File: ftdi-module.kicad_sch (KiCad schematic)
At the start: 49 parts, among them J1 USB3106-30-0230-A, U2 ISO1641, U3 NCP163ASN330T1G, U5 FT4232H-56Q, Y1 KX-7_12,MHz

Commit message: Loclib
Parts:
- U5: footprint antmicro-footprints:QFN-56-1EP_8x8mm_P0.5mm_EP5.5.9x5.9mm -> nuc-compute-cluster-power-breakout-footprints:QFN-56-1EP_8x8mm_P0.5mm_EP5.5.9x5.9mm; symbol antmicroInterfaceControllers:FT4232H-56Q -> nuc-compute-cluster-power-breakout:FT4232H-56Q
- WP1: footprint antmicro-footprints:Testpoint_smd_1mm -> nuc-compute-cluster-power-breakout-footprints:Testpoint_smd_1mm; symbol antmicroTestPoints:TP_SMD1MM -> nuc-compute-cluster-power-breakout:TP_SMD1MM

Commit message: Update README
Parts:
- 3V3, 3V3_USB1, 5V_USB1, SCL1, SCL_FTDI1, SDA1, SDA_FTDI1, WP1: footprint nuc-compute-cluster-power-breakout-footprints:Testpoint_smd_1mm -> d1600e-psu-breakout-board-footprints:Testpoint_smd_1mm; symbol nuc-compute-cluster-power-breakout:TP_SMD1MM -> d1600e-psu-breakout-board:TP_SMD1MM
- C1, C2: footprint nuc-compute-cluster-power-breakout-footprints:0402-cap -> d1600e-psu-breakout-board-footprints:0402-cap; symbol nuc-compute-cluster-power-breakout:C_27p_0402 -> d1600e-psu-breakout-board:C_27p_0402
- C10, C14, C15, C16, C17, C18, C3, C4, C6, C7, C8, C9: footprint nuc-compute-cluster-power-breakout-footprints:0402-cap -> d1600e-psu-breakout-board-footprints:0402-cap; symbol nuc-compute-cluster-power-breakout:C_100n_0402 -> d1600e-psu-breakout-board:C_100n_0402
- C11, C12, C13, C19, C20: footprint nuc-compute-cluster-power-breakout-footprints:0402-cap -> d1600e-psu-breakout-board-footprints:0402-cap; symbol nuc-compute-cluster-power-breakout:C_4u7_0402 -> d1600e-psu-breakout-board:C_4u7_0402
- D1: footprint nuc-compute-cluster-power-breakout-footprints:TPD2E009DRTR -> d1600e-psu-breakout-board-footprints:TPD2E009DRTR; symbol nuc-compute-cluster-power-breakout:PESD5V0S2BQA -> d1600e-psu-breakout-board:PESD5V0S2BQA
- D2: footprint nuc-compute-cluster-power-breakout-footprints:LED_0603 -> d1600e-psu-breakout-board-footprints:LED_0603; symbol nuc-compute-cluster-power-breakout:LG_L29K-G2J1-24-Z -> d1600e-psu-breakout-board:LG_L29K-G2J1-24-Z
- FB1, FB2, FB3: footprint nuc-compute-cluster-power-breakout-footprints:0603 -> d1600e-psu-breakout-board-footprints:0603; symbol nuc-compute-cluster-power-breakout:BLM18AG601SN1D -> d1600e-psu-breakout-board:BLM18AG601SN1D
- J1: footprint nuc-compute-cluster-power-breakout-footprints:usb3106-30-0230 -> d1600e-psu-breakout-board-footprints:usb3106-30-0230; symbol nuc-compute-cluster-power-breakout:USB3106-30-0230-A -> d1600e-psu-breakout-board:USB3106-30-0230-A
- R1: footprint nuc-compute-cluster-power-breakout-footprints:0402-res -> d1600e-psu-breakout-board-footprints:0402-res; symbol nuc-compute-cluster-power-breakout:R_1k_0402 -> d1600e-psu-breakout-board:R_1k_0402
- R3: footprint nuc-compute-cluster-power-breakout-footprints:0402-res -> d1600e-psu-breakout-board-footprints:0402-res; symbol nuc-compute-cluster-power-breakout:R_12k_0402 -> d1600e-psu-breakout-board:R_12k_0402
- R36, R37, R5, R6: footprint nuc-compute-cluster-power-breakout-footprints:0402-res -> d1600e-psu-breakout-board-footprints:0402-res; symbol nuc-compute-cluster-power-breakout:R_1k5_0402 -> d1600e-psu-breakout-board:R_1k5_0402
- R38, R39, R4, R42, R8: footprint nuc-compute-cluster-power-breakout-footprints:0603-res -> d1600e-psu-breakout-board-footprints:0603-res; symbol nuc-compute-cluster-power-breakout:R_0R_0603 -> d1600e-psu-breakout-board:R_0R_0603
- R7: footprint nuc-compute-cluster-power-breakout-footprints:0402-res -> d1600e-psu-breakout-board-footprints:0402-res; symbol nuc-compute-cluster-power-breakout:R_330R_0402 -> d1600e-psu-breakout-board:R_330R_0402
- U2: footprint nuc-compute-cluster-power-breakout-footprints:SOIC-8_W3.9mm -> d1600e-psu-breakout-board-footprints:SOIC-8_W3.9mm; symbol nuc-compute-cluster-power-breakout:ISO1641 -> d1600e-psu-breakout-board:ISO1641
- U3: footprint nuc-compute-cluster-power-breakout-footprints:SOT-23-5 -> d1600e-psu-breakout-board-footprints:SOT-23-5; symbol nuc-compute-cluster-power-breakout:NCP163ASN330T1G -> d1600e-psu-breakout-board:NCP163ASN330T1G
- U5: footprint nuc-compute-cluster-power-breakout-footprints:QFN-56-1EP_8x8mm_P0.5mm_EP5.5.9x5.9mm -> d1600e-psu-breakout-board-footprints:QFN-56-1EP_8x8mm_P0.5mm_EP5.5.9x5.9mm; symbol nuc-compute-cluster-power-breakout:FT4232H-56Q -> d1600e-psu-breakout-board:FT4232H-56Q
- Y1: footprint nuc-compute-cluster-power-breakout-footprints:KX-7 -> d1600e-psu-breakout-board-footprints:KX-7; symbol nuc-compute-cluster-power-breakout:KX-7_12,MHz -> d1600e-psu-breakout-board:KX-7_12,MHz
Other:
- note added: "Filtering"
- note added: "I2C separation"
- note removed: "Filtration"
- note removed: "Transmission Lines Separation"
- company: Antmicro Ltd. -> (none)
- title: NUC Computer Cluster Power Breakout HW -> D1600E PSU Breakout Board

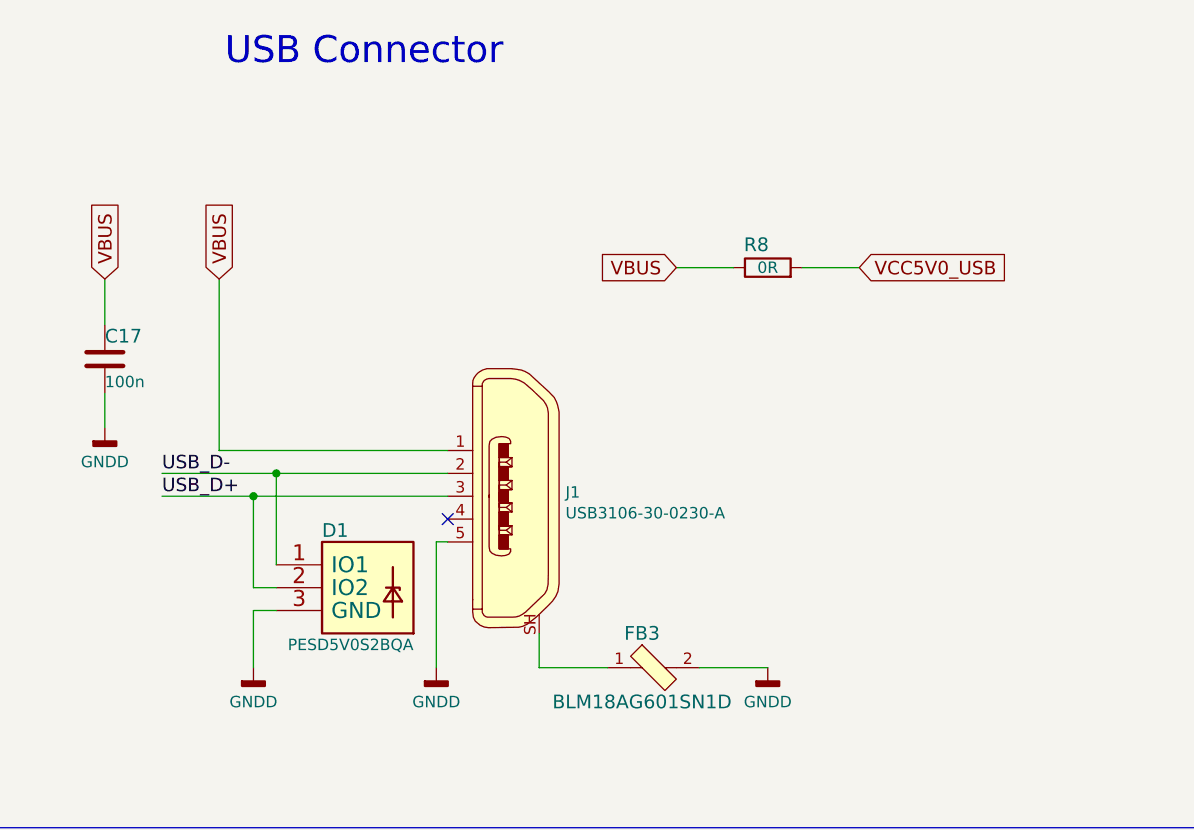
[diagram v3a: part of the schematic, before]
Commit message: Replaced usb micro to USB C
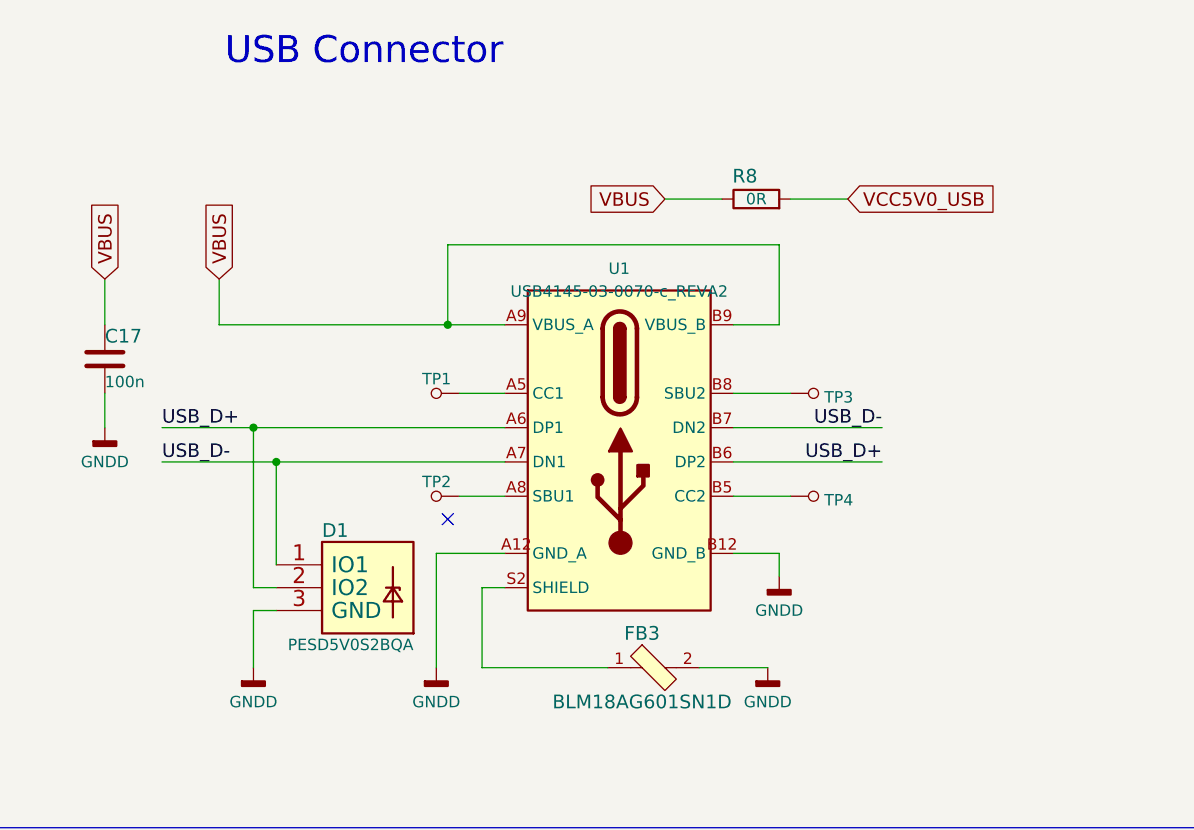
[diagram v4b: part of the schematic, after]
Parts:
- removed J1: USB3106-30-0230-A, d1600e-psu-breakout-board-footprints:usb3106-30-0230, symbol d1600e-psu-breakout-board:USB3106-30-0230-A
- added TP1, TP2, TP3, TP4: TP_SMD1MM, antmicro-footprints:Testpoint_smd_1mm, symbol antmicroTestPoints:TP_SMD1MM
- added U1: USB4145-03-0070-c_REVA2, antmicro-footprints:GCT_USB4145-03-0070-C_REVA, symbol antmicroUSBDVIHDMIConnectors:USB4145-03-0070-c_REVA
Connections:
- net GNDD: now also U1.A12 (GND_A), U1.B12 (GND_B)
- net USB_D+: now also U1.A6 (DP1), U1.B6 (DP2)
- net USB_D-: now also U1.A7 (DN1), U1.B7 (DN2)
- net VBUS: now also U1.A9 (VBUS_A), U1.B9 (VBUS_B)
- net at FB3.1: now also U1.S2 (SHIELD)
- new net: TP1.1, U1.A5 (CC1)
- new net: TP2.1, U1.A8 (SBU1)
- new net: TP4.1, U1.B5 (CC2)
- new net: TP3.1, U1.B8 (SBU2)
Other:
- moved on the sheet: R8

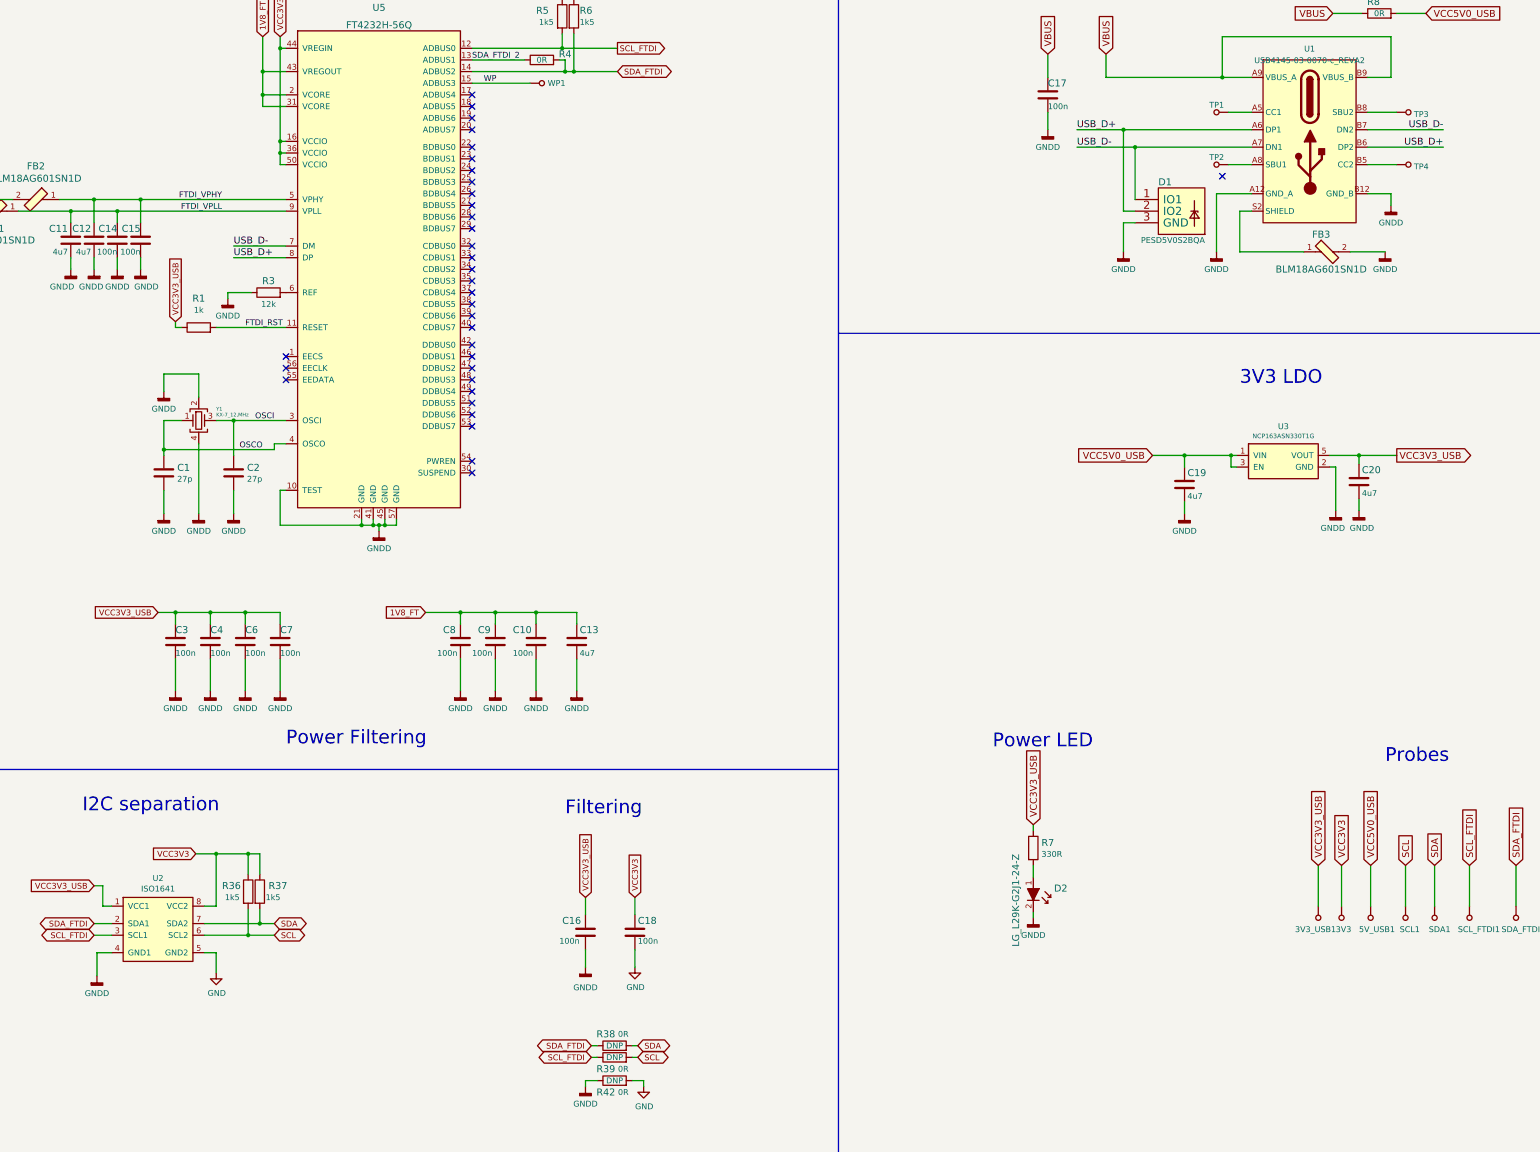
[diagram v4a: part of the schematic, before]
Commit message: Added protection for I2C, fix resistor value for USB C, Fixed J9 reversed polarity, minor width fix to 3v3 line
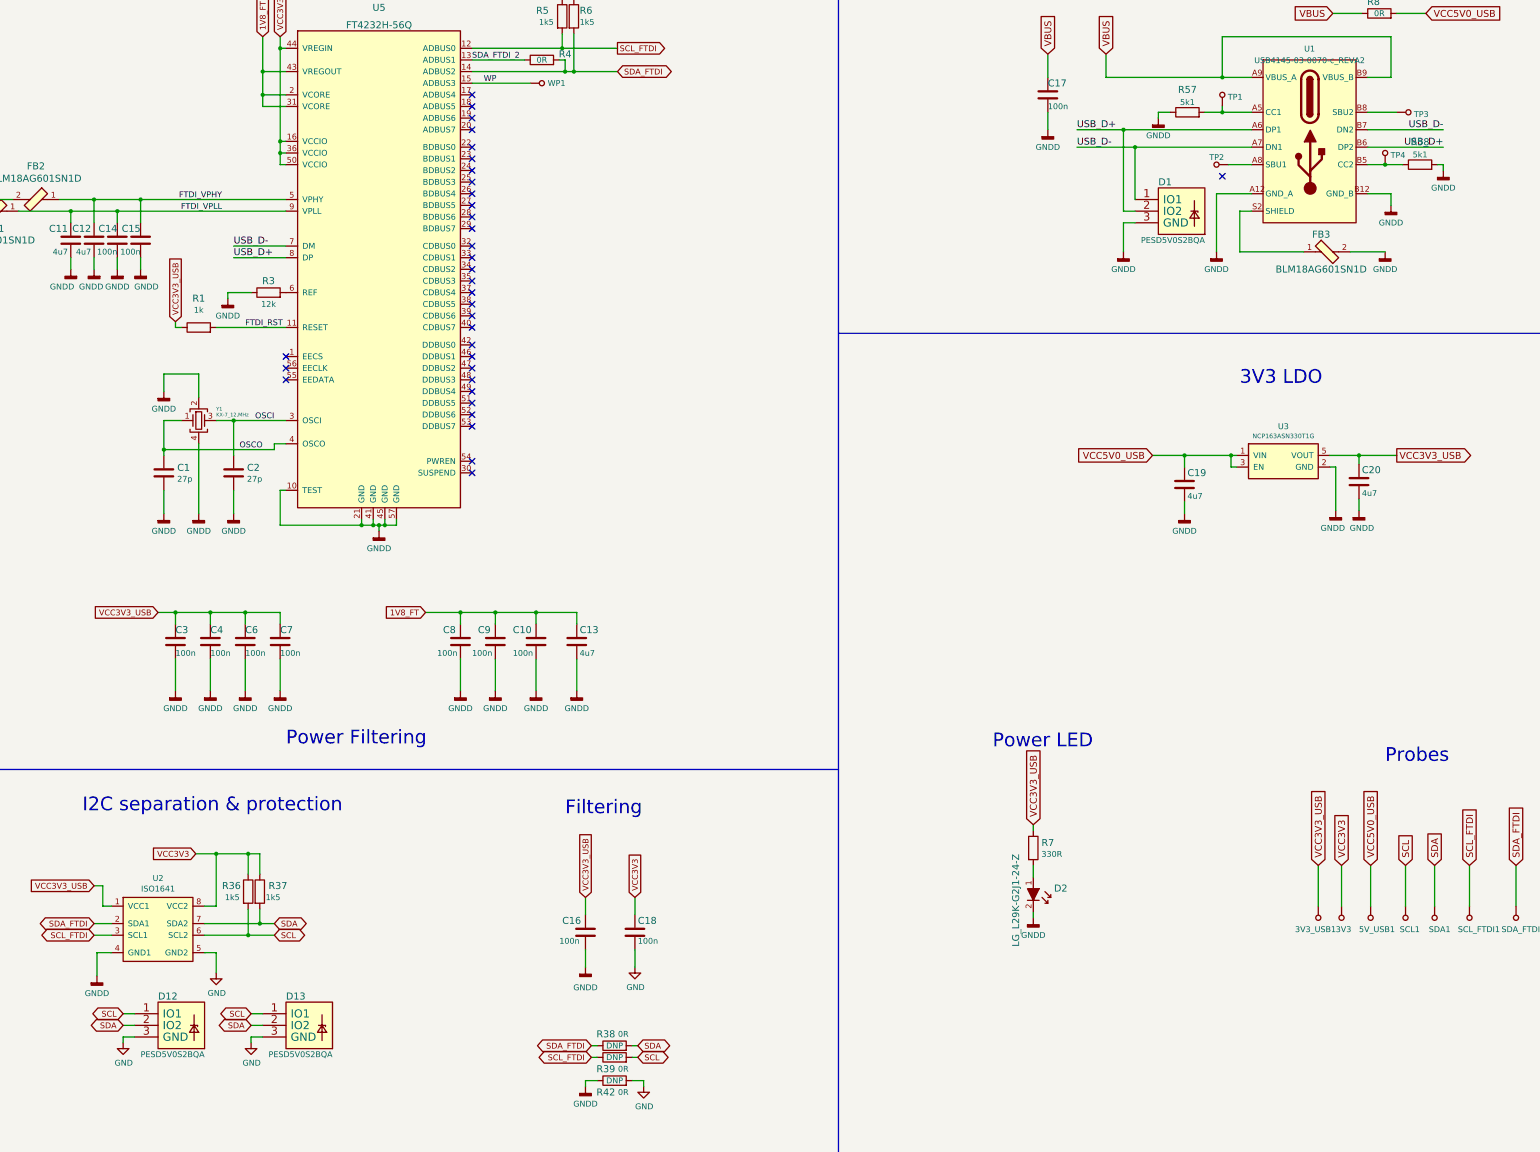
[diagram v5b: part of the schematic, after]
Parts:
- added D12, D13: PESD5V0S2BQA, d1600e-psu-breakout-board-footprints:TPD2E009DRTR, symbol d1600e-psu-breakout-board:PESD5V0S2BQA
- added R57, R58: R_5k1_0402, antmicro-footprints:0402-res, symbol antmicroResistors0402:R_5k1_0402
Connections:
- net GND: now also D12.3 (GND), D13.3 (GND)
- net GNDD: now also R57.1, R58.2
- net SCL: now also D12.1 (IO1), D13.1 (IO1)
- net SDA: now also D12.2 (IO2), D13.2 (IO2)
- net at TP1.1, U1.A5 (CC1): now also R57.2
- net at TP4.1, U1.B5 (CC2): now also R58.1
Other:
- note added: "I2C separation & protection"
- note removed: "I2C separation"
- moved on the sheet: TP1, TP4

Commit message: Added some changes after 1st review
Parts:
- removed C1, C2: C_27p_0402, d1600e-psu-breakout-board-footprints:0402-cap, symbol d1600e-psu-breakout-board:C_27p_0402
- removed D12, D13: PESD5V0S2BQA, d1600e-psu-breakout-board-footprints:TPD2E009DRTR, symbol d1600e-psu-breakout-board:PESD5V0S2BQA
- removed R36, R37, R5, R6: R_1k5_0402, d1600e-psu-breakout-board-footprints:0402-res, symbol d1600e-psu-breakout-board:R_1k5_0402
- added C1, C2: C_18p_0402, antmicro-footprints:0402-cap, symbol antmicroCapacitors0402:C_18p_0402
- added D14: PESD5V0S2BQA, d1600e-psu-breakout-board-footprints:TPD2E009DRTR, symbol d1600e-psu-breakout-board:PESD5V0S2BQA
- added R36, R37, R5, R6: R_4k7_0402, antmicro-footprints:0402-res, symbol antmicroResistors0402:R_4k7_0402
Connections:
- net GNDD: now also C1.2, C2.2, D14.3 (GND)
- net OSCI: now also C2.1
- net OSCO: now also C1.1
- net SCL: now also R36.1
- net SCL_FTDI: now also R5.1
- net SDA: now also R37.1
- net SDA_FTDI: now also R6.1
- net VBUS: now also D14.1 (IO1), D14.2 (IO2)
- net VCC3V3: now also R36.2, R37.2
- net VCC3V3_USB: now also R5.2, R6.2

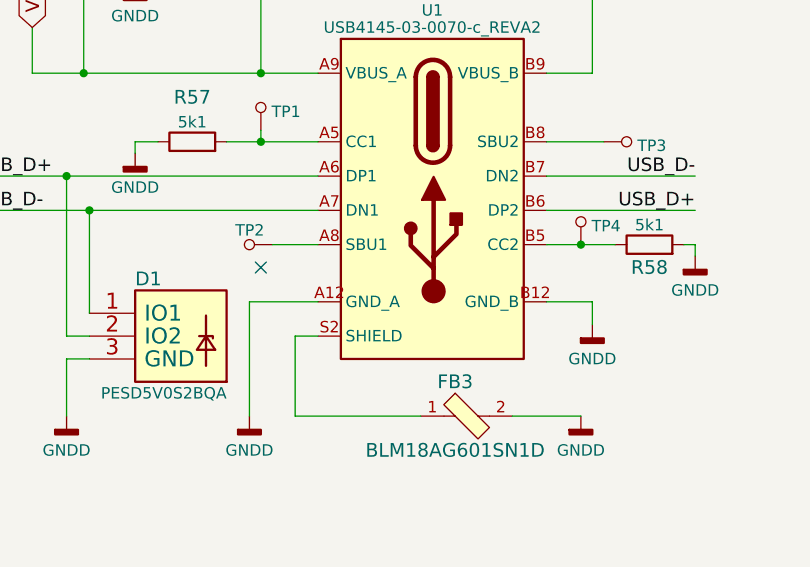
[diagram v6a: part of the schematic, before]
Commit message: Added all changes proposed in first review of the board
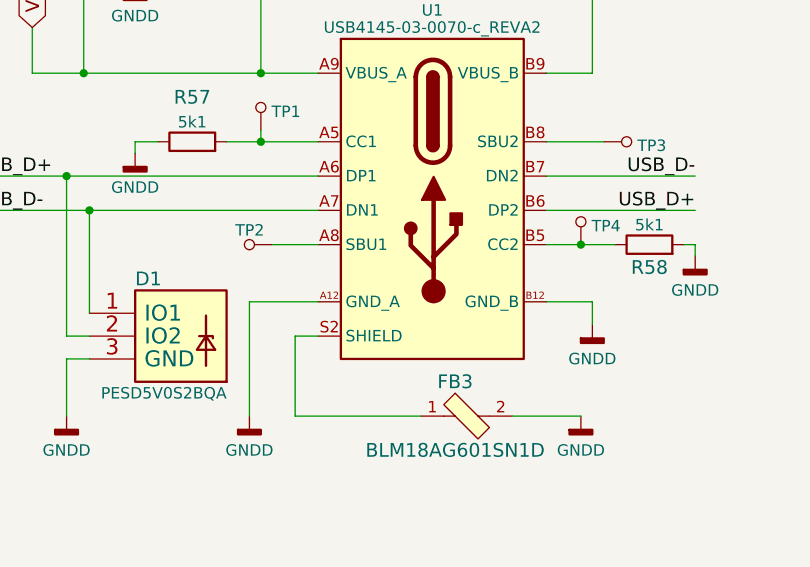
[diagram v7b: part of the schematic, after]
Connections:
- no-connect marks 34 -> 33
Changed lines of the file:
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@@
   (no_connect (at 106.68 111.76))
   (no_connect (at 106.68 109.22))
-  (no_connect (at 311.15 69.85))
   (no_connect (at 147.32 132.08))
   (no_connect (at 147.32 134.62))
